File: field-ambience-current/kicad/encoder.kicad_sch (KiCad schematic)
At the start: 9 parts, among them J4 SWD 1.27mm (SWCLK/GND/SWDIO), SW11 Reset 6mm SMD, SW12 BOOTSEL 6mm SMD (DNP for THT-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, U1 Raspberry_Pi_Pico2 (RP2350)

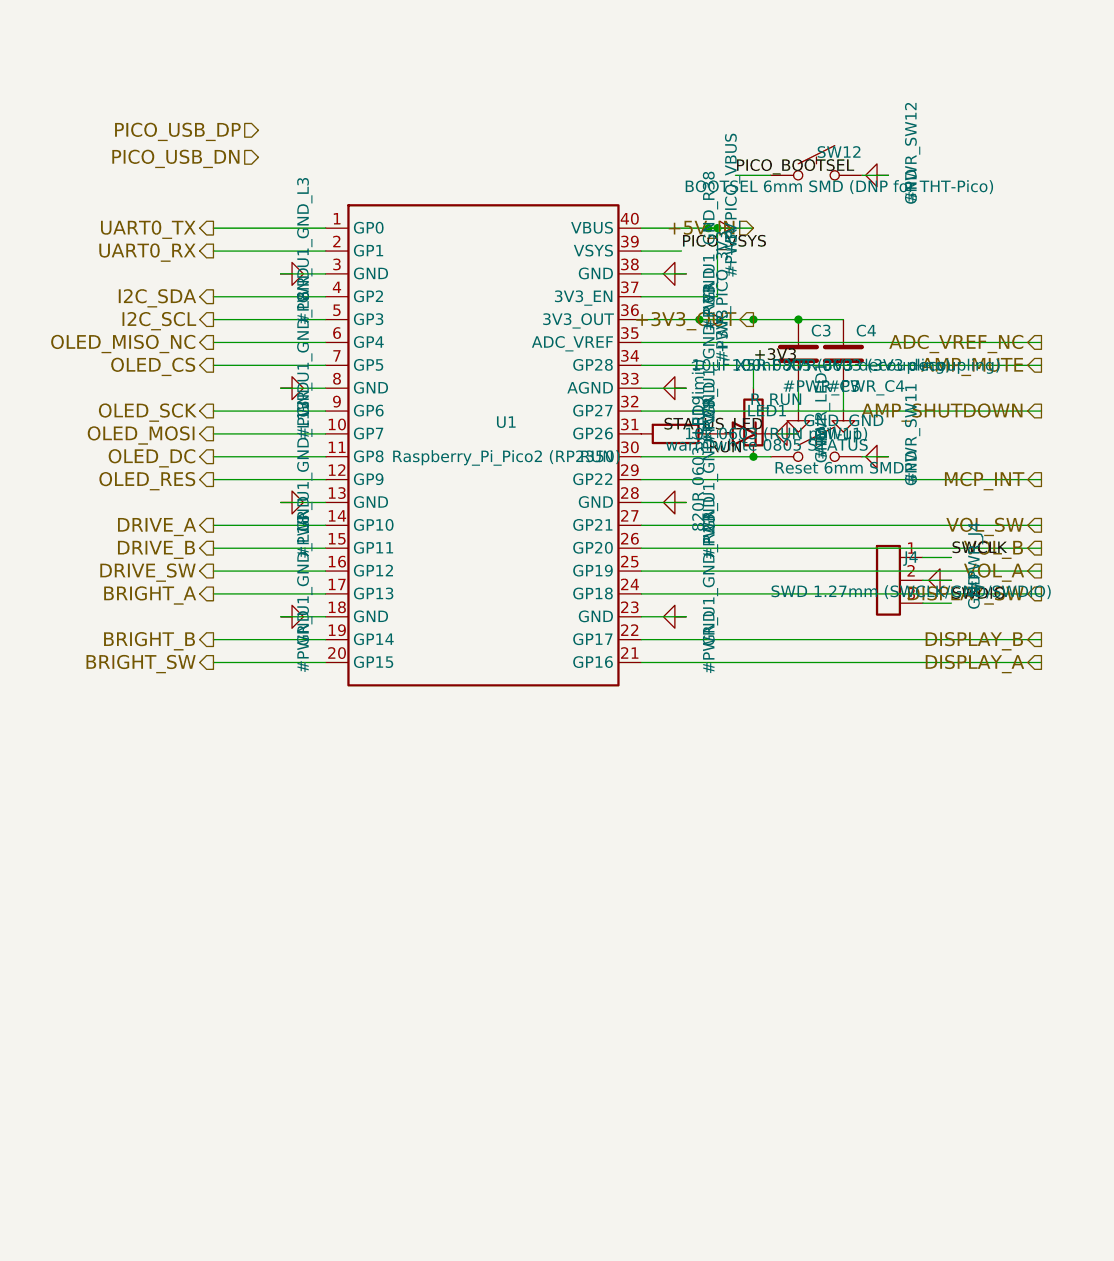
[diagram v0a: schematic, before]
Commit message: Add Sheet 5 (4x EC11 Encoder + RC-Debounce) per SPEC v0.6 §5/§M4
4 EC11-Encoder mit Push-Switch + Pull-Ups + Debounce-Caps:
- EN1 Drive (GP10/11/12)
- EN2 Brightness (GP13/14/15)
- EN3 Display (GP16/17/18)
- EN4 Volume (GP19/20/21)

Per encoder:
- A-Pin: R pull-up 10k zu +3V3, C debounce 100nF zu GND (v0.6 M4 Fix)
- B-Pin: R pull-up 10k, C debounce 100nF
- C-Pin: direkt zu GND (Common)
- SW1-Pin: R pull-up 10k, Hier-Output zu Pico
- SW2-Pin: direkt zu GND

BOM Sheet 5: 12× R 10k (8 für A/B-Pull-Ups R7-R14 + 4 für SW R15-R18),
8× C 100nF (Debounce C10-C17), 4× EC11 Encoder.

Root sheet umstrukturiert für Layout-Platz:
- Pico-Box erweitert von (60, 60) auf (60, 130) für 12 zusätzliche
  Encoder-Pins auf rechter Seite (y=110-165)
- MCP-Box von (130, 110) nach (130, 200) verschoben um Pico-Expansion
  Platz zu machen; I2C/INT-Labels entsprechend bei y=210-220 jetzt
- Encoder-Box bei (230, 105) size (60, 70) mit 12 input pins
- 12 direkte Wires Pico→Encoder bei y=110-165

Analyzer: 0 funktionale Errors (3 VM-001 false-positives unverändert),
23 warnings (von 35 gefallen, da Encoder-Signale jetzt 2-pin nets sind).
61 components total, 70 nets, 16 caps + 20 resistors + 16 switches.

Alle 4 EN1-EN4 pin_nets verifiziert via analyzer:
  Pin 1 (A): correct net (DRIVE_A / BRIGHT_A / DISPLAY_A / VOL_A)
  Pin 2 (B): correct net
  Pin 3 (C): GND
  Pin 4 (SW1): correct SW net
  Pin 5 (SW2): GND
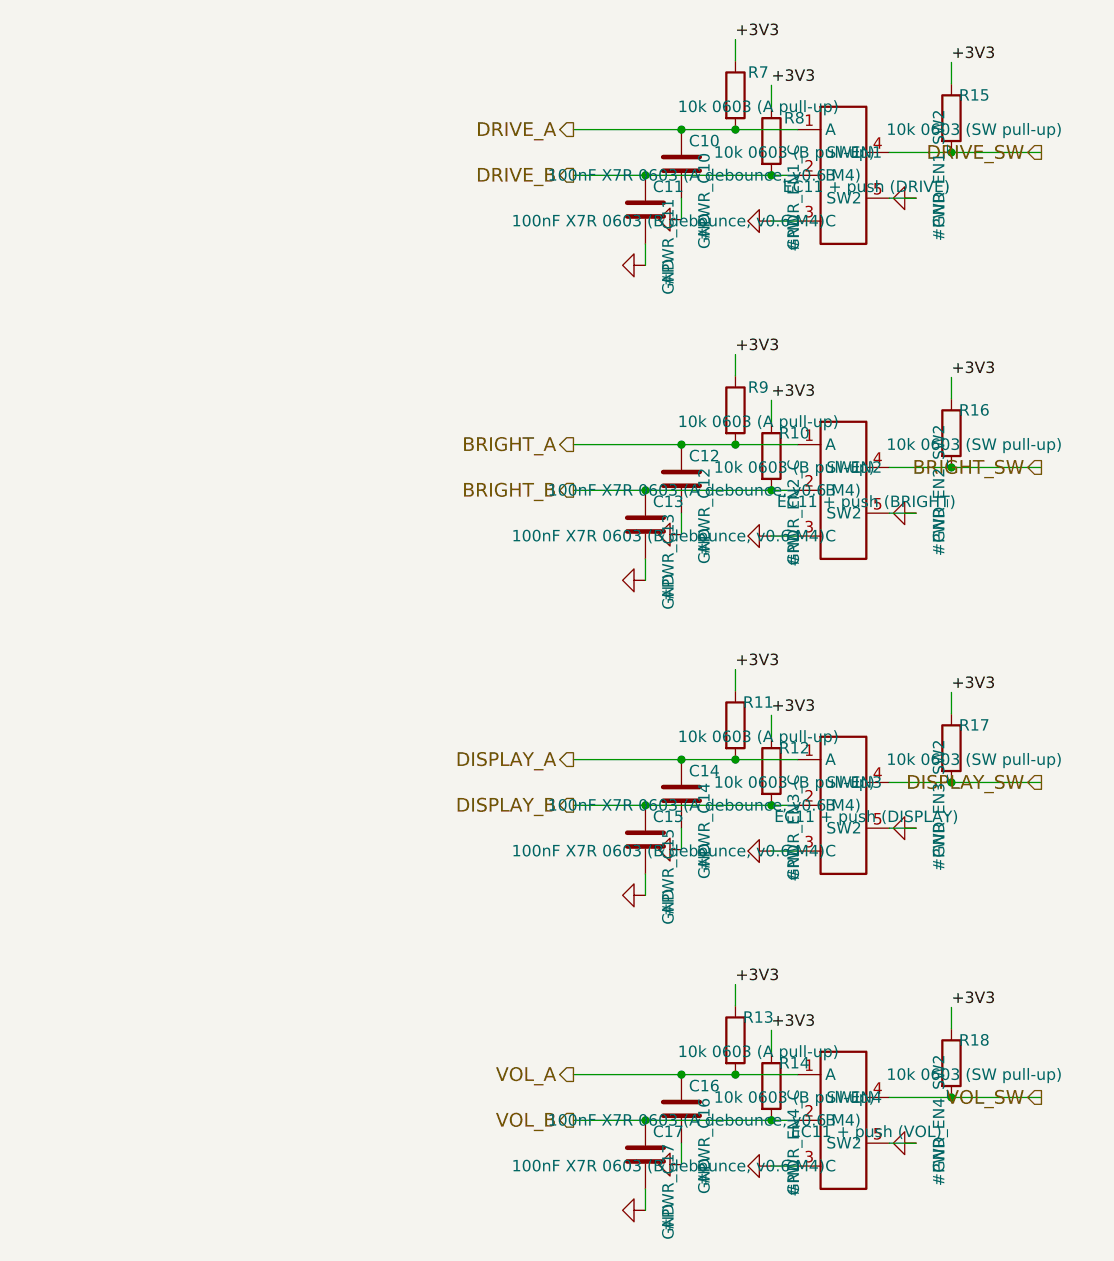
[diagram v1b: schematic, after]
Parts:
- removed C3: 10uF X5R 0805 (3V3 decoupling), Capacitor_SMD:C_0805_2012Metric, symbol Device:C
- removed C4: 100nF X7R 0603 (3V3 decoupling), Capacitor_SMD:C_0603_1608Metric, symbol Device:C
- removed J4: SWD 1.27mm (SWCLK/GND/SWDIO), Connector_PinHeader_1.27mm:PinHeader_1x03_P1.27mm_Vertical, symbol Connector:Conn_01x03
- removed LED1: warm white 0805 STATUS, LED_SMD:LED_0805_2012Metric, symbol Device:LED
- removed R19: 820R 0603 (LED limit), Resistor_SMD:R_0603_1608Metric, symbol Device:R
- removed R_RUN: 10k 0603 (RUN pull-up), Resistor_SMD:R_0603_1608Metric, symbol Device:R
- removed SW11: Reset 6mm SMD, Button_Switch_SMD:SW_SPST_TL3342, symbol Switch:SW_Push
- removed SW12: BOOTSEL 6mm SMD (DNP for THT-Pico), Button_Switch_SMD:SW_SPST_TL3342, symbol Switch:SW_Push
- removed U1: Raspberry_Pi_Pico2 (RP2350), MCU_Module:RPi_Pico_SMD_TH, symbol MCU:Pico2
- added C10, C12, C14, C16: 100nF X7R 0603 (A debounce, v0.6 M4), Capacitor_SMD:C_0603_1608Metric, symbol Device:C
- added C11, C13, C15, C17: 100nF X7R 0603 (B debounce, v0.6 M4), Capacitor_SMD:C_0603_1608Metric, symbol Device:C
- added EN1: EC11 + push (DRIVE), Rotary_Encoder:RotaryEncoder_Alps_EC11E-Switch_Vertical_H20mm, symbol Encoder:Rotary_Encoder_Switch
- added EN2: EC11 + push (BRIGHT), Rotary_Encoder:RotaryEncoder_Alps_EC11E-Switch_Vertical_H20mm, symbol Encoder:Rotary_Encoder_Switch
- added EN3: EC11 + push (DISPLAY), Rotary_Encoder:RotaryEncoder_Alps_EC11E-Switch_Vertical_H20mm, symbol Encoder:Rotary_Encoder_Switch
- added EN4: EC11 + push (VOL), Rotary_Encoder:RotaryEncoder_Alps_EC11E-Switch_Vertical_H20mm, symbol Encoder:Rotary_Encoder_Switch
- added R10, R12, R14, R8: 10k 0603 (B pull-up), Resistor_SMD:R_0603_1608Metric, symbol Device:R
- added R11, R13, R7, R9: 10k 0603 (A pull-up), Resistor_SMD:R_0603_1608Metric, symbol Device:R
- added R15, R16, R17, R18: 10k 0603 (SW pull-up), Resistor_SMD:R_0603_1608Metric, symbol Device:R
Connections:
- net +3V3: now also R10.1, R11.1, R12.1, R13.1, R14.1, R15.1, R16.1, R17.1, R18.1, R7.1, R8.1, R9.1
- net BRIGHT_A: now also C12.1, EN2.1 (A), R9.2
- net BRIGHT_B: now also C13.1, EN2.2 (B), R10.2
- net BRIGHT_SW: now also EN2.4 (SW1), R16.2
- net DISPLAY_A: now also C14.1, EN3.1 (A), R11.2
- net DISPLAY_B: now also C15.1, EN3.2 (B), R12.2
- net DISPLAY_SW: now also EN3.4 (SW1), R17.2
- net DRIVE_A: now also C10.1, EN1.1 (A), R7.2
- net DRIVE_B: now also C11.1, EN1.2 (B), R8.2
- net DRIVE_SW: now also EN1.4 (SW1), R15.2
- net GND: now also C10.2, C11.2, C12.2, C13.2, C14.2, C15.2, C16.2, C17.2, EN1.3 (C), EN1.5 (SW2), EN2.3 (C), EN2.5 (SW2), EN3.3 (C), EN3.5 (SW2), EN4.3 (C), EN4.5 (SW2)
- net VOL_A: now also C16.1, EN4.1 (A), R13.2
- net VOL_B: now also C17.1, EN4.2 (B), R14.2
- net VOL_SW: now also EN4.4 (SW1), R18.2
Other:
- title: Field Ambience PCB — Sheet 2: Pico 2 (RP2350) -> Field Ambience PCB — Sheet 5: 4x EC11 Encoder
